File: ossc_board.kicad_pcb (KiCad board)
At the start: 2 copper layers, 124.6 x 68.7 mm, 263 parts, among them J1 VGA, J2 3XRCA_CONN, J3 SCART-F, J4 HDMI_CONN, J5 5VDC_IN, J6 SJ1-3533NG, J7 SJ1-3533NG, P1 JTAG_CONN, P3 mSD_CONN, Q1 BC847, Q2 BC857, Q3 AOSS21115C, Q4 DSS20200L, Q5 AOSS21115C, SW1 SPST, SW2 SW_PUSH, SW3 SW_PUSH, SW4 GW22RCV, U1 TVP7002PZP, U10 S25FL216K, U11 IRM-V538/TR1, U12 TLV70012, U13 TLV70025, U14 TLV70012, U15 TLV70018, U16 TLV70018, U17 THS7353, U18 LM3671MF-2.5/NOPB, U2 EP4CE15E22, U3 IT6613, U4 SN74LVC2G17, U5 AP7361C, U6 TLV70033, U7 NCP703SN19T1G, U8 PCM1862, U9 TLV70019, Y1 ACHL-27MHZ-EK, Y2 24.576MHz

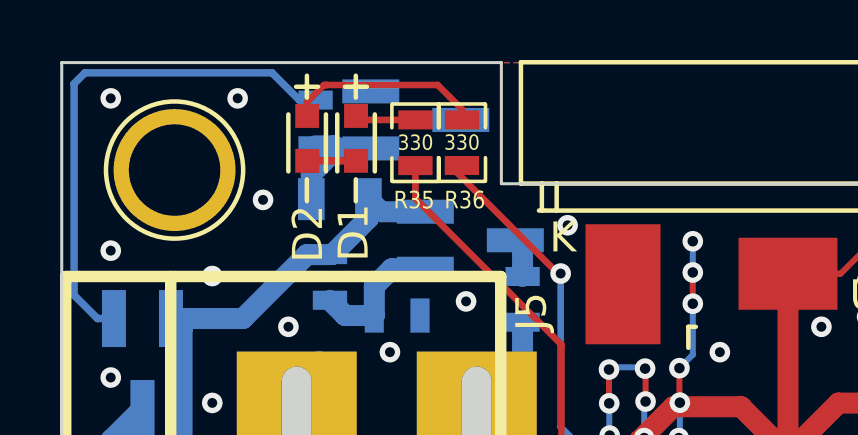
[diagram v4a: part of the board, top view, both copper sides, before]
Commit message: fix D14 footprint and add RoHS & WEEE logos
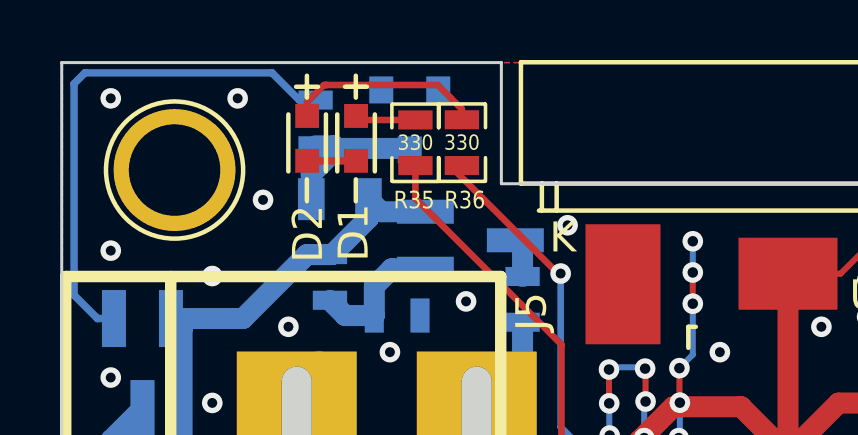
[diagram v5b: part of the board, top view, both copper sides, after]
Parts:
- added G***: WEEE-logo, custom_components:WEEE-logo, B.Cu at (67.5, 68.7)
- added G***: RoHS-logo, custom_components:RoHS-logo, B.Cu at (79.2, 68.9)
- D14: footprint Package_TO_SOT_SMD:SOT-23_Handsoldering -> Diode_SMD:D_SOT-23_ANK
- moved D14 0.20 mm to (19.0, 18.9), turned to 270 degrees
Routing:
- net Net-(D14-Pad1): track 3.92 -> 5.18 mm
